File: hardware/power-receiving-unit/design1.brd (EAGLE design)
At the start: 60 x 20 mm, 77 parts, among them IC12 NRF52832, IC2 STM32L011F3U6TR, IC3 TPS54308DDCR, IC4 MCP6486T-E/OT, Q1 BSS138, Q2 SI3481DV, U1 MAX5422ETA-T, X1 DG3XX-02-5.0, Y1 32MHz, Y2 32.768kHz

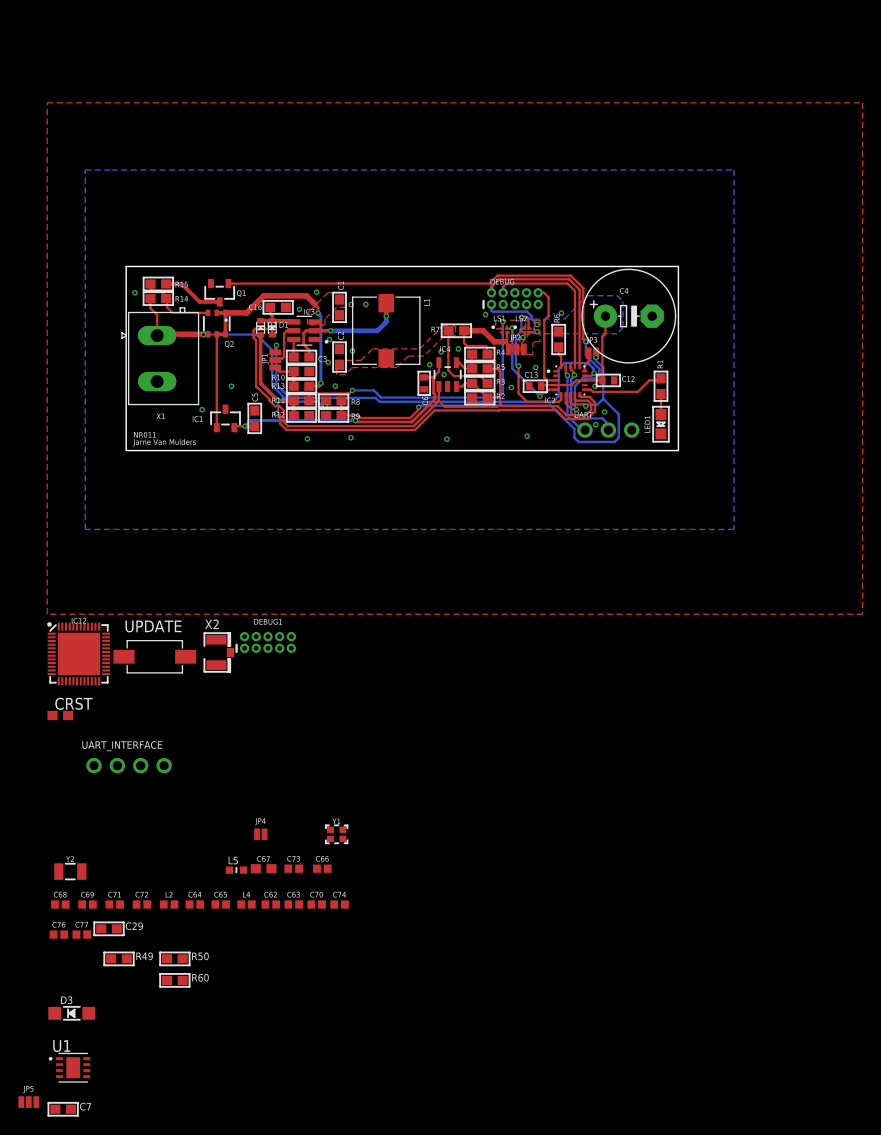
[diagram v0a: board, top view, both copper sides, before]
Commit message: draft scheme power-receiving-unit
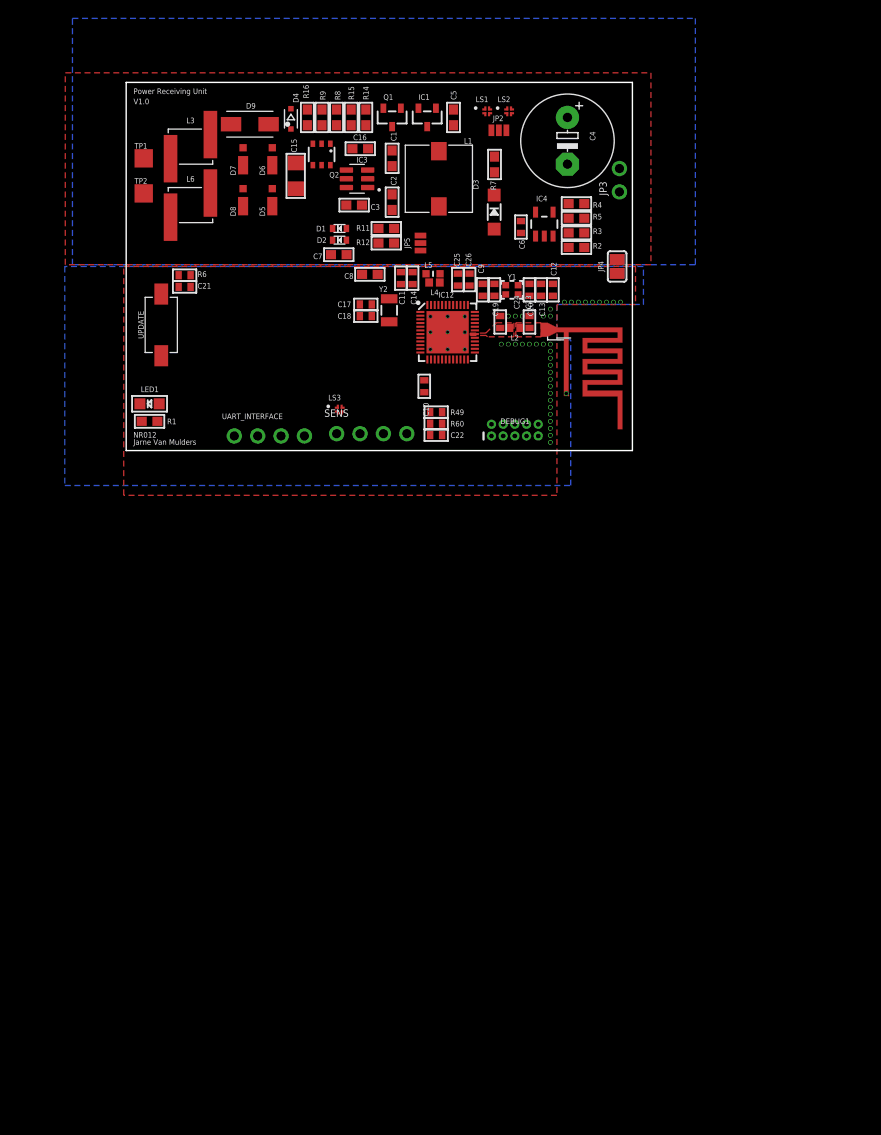
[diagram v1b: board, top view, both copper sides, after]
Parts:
- removed C29: 100n, microbuilder:0603
- removed C62, C63: 6pF, nrf52832-breakout-temp:0402
- removed C64, C65: 15pF, SparkFun-Capacitors:0402
- removed C66, C68, C69: 0.1uF, SparkFun-Capacitors:0402
- removed C67: 4.7uF, SparkFun-Capacitors:0603
- removed C70, C74: DNP, SparkFun-Passives:0402
- removed C71: 1.0uF, SparkFun-Capacitors:0402
- removed C72: 0.8pF, nrf52832-breakout-temp:0402
- removed C73: 100pF, nrf52832-breakout-temp:0402
- removed C76, C77: 12p, SparkFun-Capacitors:0402
- removed CRST: 100n, rcl:C0603
- removed DEBUG: CORTEX_DEBUGPTH, SparkFun-Connectors:2X5-PTH-1.27MM
- removed IC2: STM32L011F3U6TR, STM32L011F3U6TR:QFN50P300X300X60-21N
- removed R10, R50: 10k, microbuilder:0603
- removed R13: 100k, microbuilder:0603
- removed U1: MAX5422ETA-T, MAX5422ETA-T:SON65P300X300X80-9N
- removed UART: (no value), microbuilder:1X03_ROUND
- removed X1: DG3XX-02-5.0, degson:DG306-5.0-02P
- removed X2: (no value), adafruit:U.FL
- added C10, C11, C21, C22, C9: 100n, microbuilder:0402
- added C14: 1u, microbuilder:0402
- added C15: 10u, microbuilder:1206
- added C17, C18: 15p, microbuilder:0402
- added C19, C20: 6p, microbuilder:0402
- added C23: DNP, microbuilder:0402
- added C24: 0.8p, microbuilder:0402
- added C25, C26: 12p, microbuilder:0402
- added C8: 4u7, microbuilder:0603
- added D4: MM3Z3V0T1G, diode:SOD323-R
- added D5, D6, D7, D8: PD3S160, diode:POWERDI323
- added D9: SMAJ30A, SMAJ30A:DIOM5026X229N
- added L3, L6: (no value), PowerMagnetics (rev18e):WE-CAIR_4248
- added LS3: MIC94081YFT-TR, MIC94081YFT-TR:IC_MIC94081YFT-TR
- added R16: 47k, microbuilder:0603
- added SENS: (no value), microbuilder:1X04_ROUND
- added TP1, TP2: TPTP20SQ, testpad:TP20SQ
- added U$18: BLE-ANT, ble-antenna:ANT-2G4
- C12: value 100n -> DNP
- C13: value 100n -> 100p
- JP1: value JUMPER-SMT_3_NO_NO-SILK -> (none); device SparkFun-Jumpers:SMT-JUMPER_3_NO_NO-SILK -> microbuilder:SOLDERJUMPER_REFLOW_NOPASTE
- JP3: value JUMPER-SMT_2_NO_NO-SILK -> (none); device SparkFun-Jumpers:SMT-JUMPER_2_NO_NO-SILK -> microbuilder:1X02_ROUND
- JP4: value JUMPER-SMT_2_NO_NO-SILK -> (none); device SparkFun-Jumpers:SMT-JUMPER_2_NO_NO-SILK -> microbuilder:SOLDERJUMPER_REFLOW_NOPASTE
- R49, R60: device microbuilder:0603 -> microbuilder:0402
- R6: value 100k -> 10k; device microbuilder:0603 -> microbuilder:0402
- moved JP5 102.6 mm to (32.0, 22.5), turned to 90 degrees
- moved D3 98.4 mm to (40.0, 25.9), turned to 270 degrees
- moved C7 97.6 mm to (23.1, 21.3), turned to 180 degrees
- moved L2 73.0 mm to (42.2, 13.3), turned to 180 degrees
- moved JP4 72.8 mm to (53.3, 20.0), turned to 270 degrees
- moved L4 70.6 mm to (33.5, 18.3), turned to 180 degrees
- moved Y2 70.1 mm to (28.6, 15.2), turned to 90 degrees
- moved R49 68.7 mm to (33.7, 4.17)
- moved L5 68.2 mm to (33.3, 19.2)
- moved R60 66.8 mm to (33.7, 2.92)
- moved Y1 62.1 mm to (41.9, 17.5)
- moved R1 55.7 mm to (2.54, 3.17), turned to 0 degrees
- moved LED1 55.6 mm to (2.54, 5.08), turned to 90 degrees
- moved IC12 53.2 mm to (34.9, 12.9)
- moved R6 41.2 mm to (6.35, 19.1), turned to 0 degrees
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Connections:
- net P18 renamed SWO/TDO
- removed net N$1: JP1.1, R10.1, R13.2
- removed net N$10: Q2.4, R14.1, R8.1, X1.1
- removed net N$11: IC2.15, JP3.1
- removed net N$45: C74.1, L2.1, X2.3
- removed net N$7: IC3.5, JP1.2
- removed net NRST: DEBUG.10, IC2.3
- removed net P15: IC12.18
- removed net P19: IC12.22
- removed net P20: IC12.23
- removed net P26: C76.2, IC12.38
- removed net P27: IC12.39
- removed net PB9: IC2.20, R6.1
- removed net USART2_RX: IC2.19, UART.1
- removed net USART2_TX: IC2.18, UART.2
- removed net VDD-AUX-EN: IC2.1
- new net AGND: C1.2, C15.2, C16.1, C2.2, C4.-, C5.2, C6.2, C7.2, D4.A, D6.A, D7.A, D9.A, IC1.3, IC3.1, IC4.2, JP1.1, JP3.2, JP5.1, LS1.2, LS2.2, Q1.2, R2.1, R9.2
- new net EN_SENS: IC12.23, LS3.4
- new net I2C_SCL: IC12.39, SENS.3
- new net I2C_SDA: C25.1, IC12.38, SENS.2
- new net MIFA: C23.1, L2.1, U$18.1
- new net N$12: L6.1, TP2.TP
- new net N$14: L3.1, TP1.TP
- new net N$15: D5.A, D6.C, L3.2
- new net N$16: D7.C, D8.A, L6.2
- new net VDD_SENS: LS3.1, SENS.1
- new net VDD_WPT: C15.1, D5.C, D8.C, D9.C, Q2.4, R14.1, R16.1, R8.1
- new net WAKE-UP: D4.C, IC12.22, R16.2
- net !RESET!: now also C22.1; no longer CRST.1
- net 3.3V: no longer U1.1
- net ADC1: no longer IC2.8, JP3.2
- net ANT: now also C24.1; no longer C72.2
- net BUCK_EN: now also IC3.5; no longer IC2.14, JP1.3
- net DEC4: now also C14.2; no longer C71.2
- net DEC5: now also C11.2; no longer C69.2
- net DEC6: now also C12.2; no longer C70.2
- net DEC8: now also C13.2; no longer C73.2
- net EN1: no longer IC2.5
- net EN2: no longer IC2.6
- net GND: now also C10.2, C11.1, C12.1, C13.1, C14.1, C17.2, C18.2, C19.1, C20.1, C21.2, C22.2, C23.2, C24.2, C25.2, C26.2, C8.2, C9.2, JP1.2, LS3.2, SENS.4, U$18.2; no longer C1.2, C12.2, C13.2, C16.1, C2.2, C29.2, C4.-, C5.2, C6.2, C62.1, C63.2, C64.1, C65.1, C66.2, C67.2, C68.2, C69.1, C7.2, C70.1, C71.1, C72.1, C73.1, C74.2, C76.1, C77.1, CRST.2, DEBUG.3, DEBUG.5, DEBUG.9, IC1.3, IC2.12, IC3.1, IC4.2, JP5.1, LS1.2, LS2.2, Q1.2, R10.2, R2.1, R6.2, R9.2, U1.5, U1.9, UART.3, X1.2, X2.1, X2.2
- net LED: now also IC12.18; no longer IC12.20, IC2.11
- net N$50: now also C26.1; no longer C77.2
- net P00: now also C17.1; no longer C64.2
- net P01: now also C18.1; no longer C65.2
- net P16: now also C21.1, R6.1; no longer C29.1, R50.1
- net PG: no longer IC2.7
- net PWM-CHG: now also IC12.20
- net SWDCLK: no longer DEBUG.4, IC2.17
- net SWDIO: no longer DEBUG.2, IC2.16
- net V-ICHG: no longer IC2.9
- net V-VCHG: no longer IC2.10
- net VCHG: now also JP3.1; no longer C12.1, C13.1, DEBUG.1, IC2.13, IC2.4
- net VDD_BLE: now also C10.1, C8.1, C9.1, LS3.3, R6.2; no longer C66.1, C67.1, C68.1, R50.2
- net VIN: no longer R13.1
- net XC1: now also C20.2; no longer C62.2
- net XC2: now also C19.2; no longer C63.1
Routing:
- net V-ICHG: track 59.8 -> 0.00 mm
- net PG: track 57.9 -> 0.00 mm, vias 2 -> 0
- net V-VCHG: track 53.3 -> 0.00 mm, vias 2 -> 0
- net ADC1: track 50.0 -> 0.00 mm, vias 3 -> 0
- net BUCK_EN: track 45.8 -> 0.00 mm, vias 2 -> 0
- net VIN: track 35.6 -> 0.00 mm, vias 2 -> 0
- net 3.3V: track 30.7 -> 0.00 mm, vias 2 -> 0
- net VMEAS: track 30.2 -> 0.00 mm, vias 2 -> 0
- net N$10: track 29.7 -> 0.00 mm, vias 2 -> 0
- net VCHG: track 21.4 -> 0.00 mm, vias 2 -> 0
- net SWDIO: track 19.3 -> 0.00 mm
- net SWDCLK: track 17.1 -> 0.00 mm
- net EN2: track 16.2 -> 0.00 mm, vias 2 -> 0
- net N$3: track 14.4 -> 0.00 mm, vias 2 -> 0
- net BUCK-OUT-2: track 11.9 -> 0.00 mm
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- added copper zone on layer 1, net AGND
- added copper zone on layer 16, net AGND
- added copper zone on layer 1, net ANT
- added copper zone on layer 1, net MIFA
- removed copper zone on layer 1, net BUCK-OUT-1
- removed copper zone on layer 1, net VCHG
- removed copper zone on layer 16, net VCHG
- removed copper zone on layer 1, net VIN
- removed copper zone on layer 1, net VMEAS
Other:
- board size 60 x 20 mm -> 55 x 40 mm
- board text added: "NR012"
- board text added: "Power Receiving Unit"
- board text added: "V1.0"
- board text removed: "NR011"

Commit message: power receiving unit PCB V1.0 ready
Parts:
- removed SENS: (no value), microbuilder:1X04_ROUND
- added C27, C28, C29: 100n, microbuilder:0402
- added JP10, JP11, JP12, JP13, JP14, JP6, JP7, JP8, JP9: JUMPER-SMT_2_NO_NO-SILK, SparkFun-Jumpers:SMT-JUMPER_2_NO_NO-SILK
- added SENSOR: (no value), microbuilder:1X04_ROUND
- moved C10 4.27 mm to (29.4, 10.0), turned to 180 degrees
- moved C1 0.67 mm to (28.4, 32.2), turned to 90 degrees
- moved C8 0.64 mm to (27.1, 19.1)
- moved L4 0.16 mm to (33.5, 18.1)
- turned C14 to 90 degrees
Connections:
- new net P02: C27.1, IC12.4, JP12.1
- new net P03: C28.1, IC12.5, JP13.1
- new net P04: C29.1, IC12.6, JP14.1
- new net P11: IC12.14, JP6.1
- new net P12: IC12.15, JP7.1
- new net P13: IC12.16, JP8.1
- new net P14: IC12.17, JP9.1
- new net P17: IC12.20, JP10.1
- new net P19: IC12.22, JP11.1
- net ADC1: now also JP12.2; no longer IC12.4
- net BUCK_EN: now also JP8.2; no longer IC12.16
- net EN1: now also JP6.2; no longer IC12.14
- net EN2: now also JP7.2; no longer IC12.15
- net GND: now also C27.2, C28.2, C29.2, SENSOR.4; no longer SENS.4
- net I2C_SCL: now also SENSOR.3; no longer SENS.3
- net I2C_SDA: now also SENSOR.2; no longer SENS.2
- net PG: now also JP9.2; no longer IC12.17
- net PWM-CHG: now also JP10.2; no longer IC12.20
- net V-ICHG: now also JP14.2; no longer IC12.6
- net V-VCHG: now also JP13.2; no longer IC12.5
- net VDD_SENS: now also SENSOR.1; no longer SENS.1
- net WAKE-UP: now also JP11.2; no longer IC12.22
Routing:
- net VDD_BLE: track 0.00 -> 97.2 mm, vias 0 -> 9
- net PG: track 0.00 -> 63.2 mm, vias 0 -> 6
- net V-ICHG: track 0.00 -> 49.1 mm, vias 0 -> 7
- net EN1: track 0.00 -> 45.9 mm, vias 0 -> 6
- net P16: track 0.00 -> 43.9 mm, vias 0 -> 2
- net EN2: track 0.00 -> 43.7 mm, vias 0 -> 4
- net WAKE-UP: track 0.00 -> 37.4 mm
- net VDD_WPT: track 0.00 -> 35.9 mm, vias 0 -> 6
- net VMEAS: track 0.00 -> 35.6 mm, vias 0 -> 2
- net LED: track 0.00 -> 34.9 mm
- net P19: track 0.00 -> 34.7 mm, vias 0 -> 4
- net P17: track 0.00 -> 31.3 mm, vias 0 -> 2
- net 3.3V: track 0.00 -> 29.8 mm, vias 0 -> 4
- net ADC1: track 0.00 -> 29.2 mm, vias 0 -> 2
- net VCHG: track 0.00 -> 29.1 mm
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- added copper zone on layer 1, net N$13
- added copper zone on layer 1, net N$3
- added copper zone on layer 1, net VIN
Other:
- board text added: "CTS"
- board text added: "GND"
- board text added: "RTS"
- board text added: "RXI"
- board text added: "SCL"
- board text added: "SDA"
- board text added: "TXI"
- board text added: "VDD"

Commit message: Update SW PRU & HW PRU + PTU
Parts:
- removed IC12: NRF52832, SparkFun-RF:QFN48-6X6MM
- added IC2: (no value), SparkFun-RF:QFN48-6X6MM-EXTENDED
- C7: value 10u -> DNP
- R15: value 100k -> 15k
- R3, R4: value 1k -> 1k2
- R7: value R025 -> R020
- R9: value 4k7 -> 10k
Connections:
- removed net NC: IC12.44
- net !RESET!: now also IC2.24; no longer IC12.24
- net ANT: now also IC2.30; no longer IC12.30
- net DCC: now also IC2.47; no longer IC12.47
- net DEC4: now also IC2.46; no longer IC12.46
- net DEC5: now also IC2.1; no longer IC12.1
- net DEC6: now also IC2.32; no longer IC12.32
- net DEC8: now also IC2.33; no longer IC12.33
- net EN_SENS: now also IC2.23; no longer IC12.23
- net GND: now also IC2.31, IC2.45, IC2.EP; no longer IC12.31, IC12.45, IC12.EP
- net I2C_SCL: now also IC2.39; no longer IC12.39
- net I2C_SDA: now also IC2.38; no longer IC12.38
- net LED: now also IC2.18; no longer IC12.18
- net MISO: now also IC2.41; no longer IC12.41
- net MOSI: now also IC2.42; no longer IC12.42
- net N$50: now also IC2.37; no longer IC12.37
- net P00: now also IC2.2; no longer IC12.2
- net P01: now also IC2.3; no longer IC12.3
- net P02: now also IC2.4; no longer IC12.4
- net P03: now also IC2.5; no longer IC12.5
- net P04: now also IC2.6; no longer IC12.6
- net P05: now also IC2.7; no longer IC12.7
- net P06: now also IC2.8; no longer IC12.8
- net P07: now also IC2.9; no longer IC12.9
- net P08: now also IC2.10; no longer IC12.10
- net P09: now also IC2.11; no longer IC12.11
- net P10: now also IC2.12; no longer IC12.12
- net P11: now also IC2.14; no longer IC12.14
- net P12: now also IC2.15; no longer IC12.15
- net P13: now also IC2.16; no longer IC12.16
- net P14: now also IC2.17; no longer IC12.17
- net P16: now also IC2.19; no longer IC12.19
- net P17: now also IC2.20; no longer IC12.20
- net P19: now also IC2.22; no longer IC12.22
- net P22: now also IC2.27; no longer IC12.27
- net P23: now also IC2.28; no longer IC12.28
- net P24: now also IC2.29; no longer IC12.29
- net P28: now also IC2.40; no longer IC12.40
- net SCK: now also IC2.43; no longer IC12.43
- net SWDCLK: now also IC2.25; no longer IC12.25
- net SWDIO: now also IC2.26; no longer IC12.26
- net SWO/TDO: now also IC2.21; no longer IC12.21
- net VDD_BLE: now also IC2.13, IC2.36, IC2.48; no longer IC12.13, IC12.36, IC12.48
- net XC1: now also IC2.34; no longer IC12.34
- net XC2: now also IC2.35; no longer IC12.35
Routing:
- net GND: track 5.95 -> 1.49 mm, vias 89 -> 91
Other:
- board text added: "V1.1"
- board text removed: "V1.0"

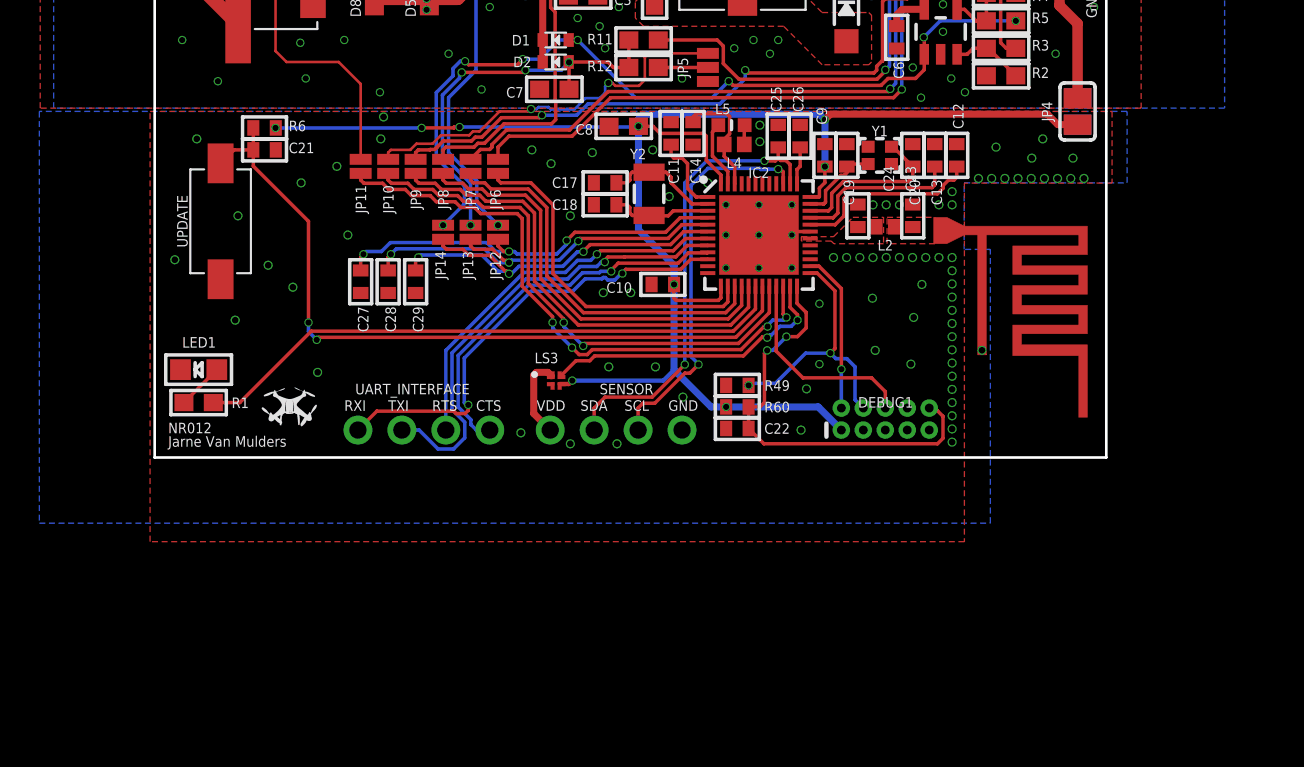
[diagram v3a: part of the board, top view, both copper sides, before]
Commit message: Update PRU HW + firmware (send pru info via BLE adv)
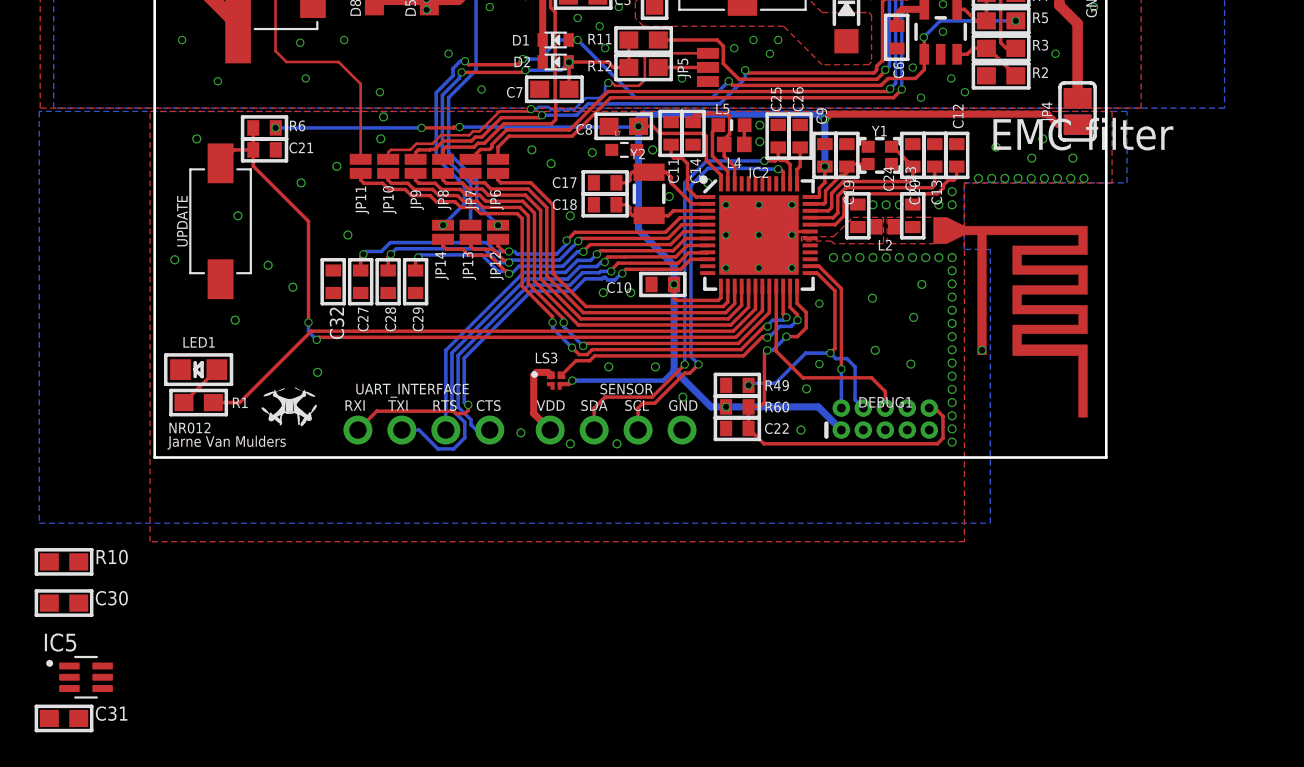
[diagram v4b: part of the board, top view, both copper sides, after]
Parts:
- added C30, C31: 100n, microbuilder:0603
- added C32: 100n, microbuilder:0402
- added IC5: (no value), TPL0401A-10DCKR:SOT65P210X110-6N
- added L7: 742792692, PowerMagnetics (rev18e):WE-CBF_0603(W=2.2)
- added R10: 100k, microbuilder:0603
- C7: value DNP -> 100n
- R2, R5: value 39k -> 56k
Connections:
- new net N$7: JP4.2, L7.1
- net 3.3V: now also C31.1, IC5.1
- net AGND: now also C30.1, C31.2, IC5.2, IC5.6
- net GND: now also C32.2
- net I2C_SCL: now also IC5.3
- net I2C_SDA: now also IC5.4
- net P19: now also C32.1
- net PWM-CHG: now also IC5.5
- net V-ICHG: now also C30.2, R10.1, R10.2
- net V-VCHG: no longer JP13.2
- net VDD_BLE: now also JP13.2, L7.2; no longer JP4.2
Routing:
- net VDD_BLE: track 97.2 -> 96.0 mm
- net V-VCHG: vias 4 -> 3
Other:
- board text added: "EMC filter"
